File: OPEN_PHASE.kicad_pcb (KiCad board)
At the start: 4 copper layers, 65 x 77.5 mm, 117 parts, among them IC1 AD7606C-18BSTZ, IC10 INA241A2IDGKR, IC2 INA241A2IDGKR, IC3 LTC6655BHMS8-2.5#PBF, IC4 INA241A2IDGKR, IC5 LT8362EMSE#PBF, IC6 INA241A2IDGKR, IC7 LTC6655BHMS8-5#PBF, IC8 LT3045EDD-1#TRPBF, IC9 LT3045EDD-1#TRPBF, J1 MR60PW, J2 MR60PW, J3 XT60PW-F, J4 PinHeader_2x08, J5 XT60PW-M

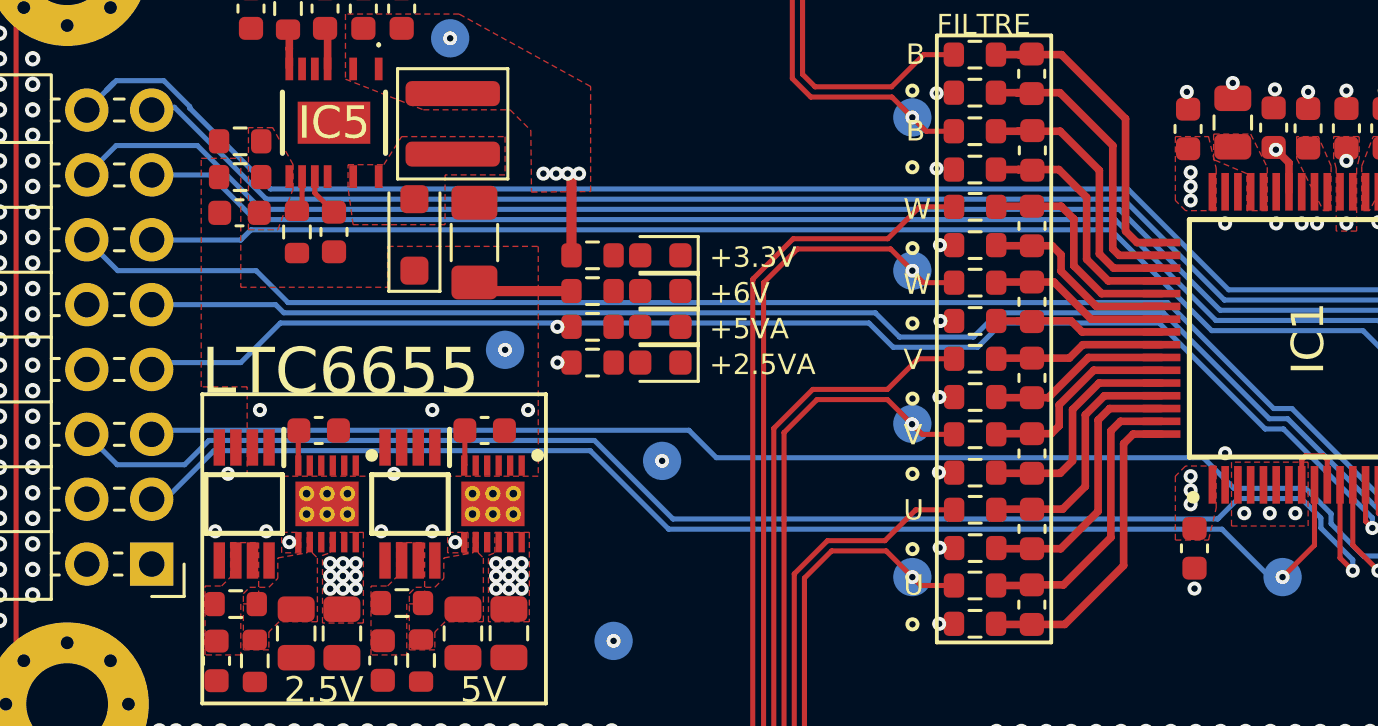
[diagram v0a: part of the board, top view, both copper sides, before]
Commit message: Add 100 Ohm series resistors on the J4 lines, bottom side
RN1, RN2 (R_Array_Concave_4x0603, the 4 x 100 Ohm array of OPEN_WEIGHT)
and R39-R41 (0603) sit inline on the existing B.Cu buses between IC1 and
J4; only the bus sections around them were redrawn. Element order follows
the routing: RN2 = DOUTD..DOUTA, R41 = SDI, RN1 = FRSTDATA, SCLK, CS,
BUSY, R40 = RESET, R39 = CONVST. J4 pinout unchanged.

Schematic: IC1 keeps its wires with local labels (IC side); the resistor
block carries the ADC_* global labels (J4 side). TP15 / TP16 move to the
IC side, where their pads are on the board.

Fixes a short: the +5VA via of R36 (138.6, 60.2) sat on the ADC_~{CS}
track; bus B now passes above it.

DRC 206 -> 203 (the short's 3 errors), parity 34 -> 16 (all pre-existing),
ERC unchanged; top and inner layers identical.

Co-Authored-By: Claude Opus 5.5 <noreply@anthropic.com>
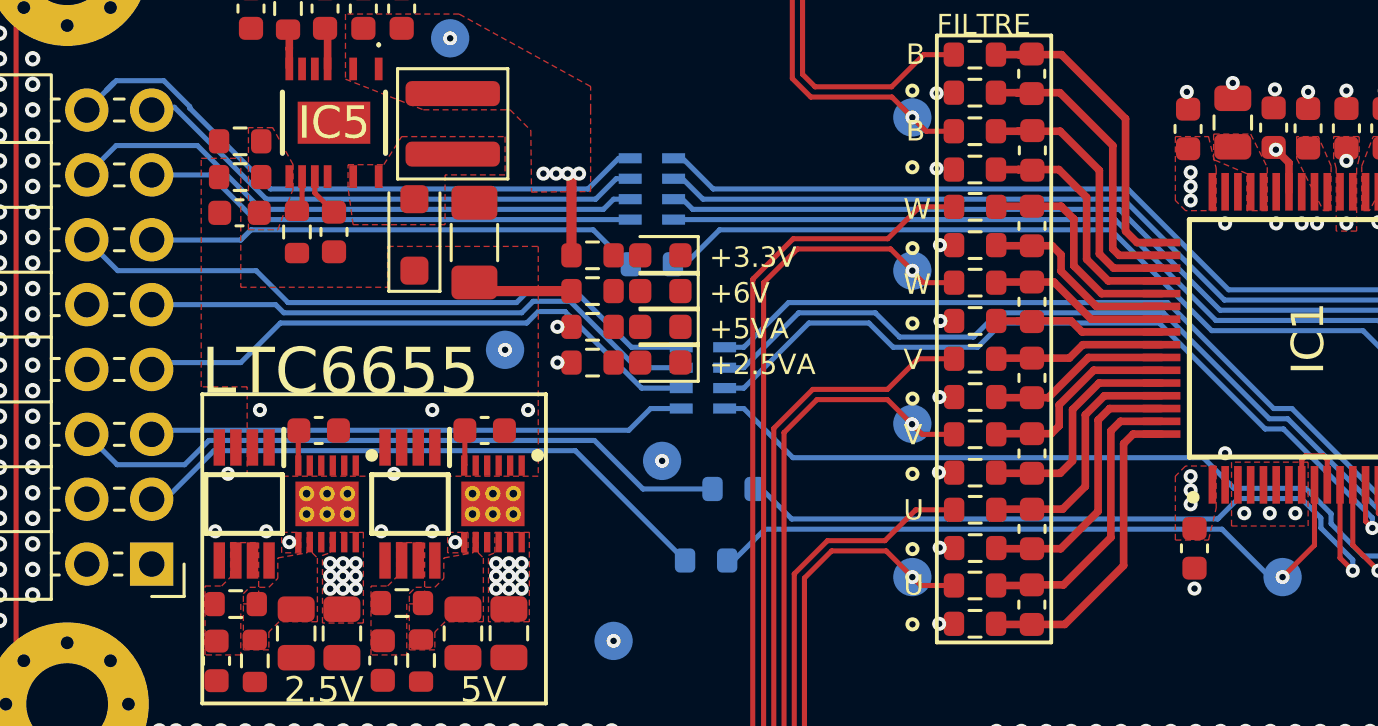
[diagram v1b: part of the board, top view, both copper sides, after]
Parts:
- added R39: 100Ω, OPEN_PHASE:R_0603_1608Metric, B.Cu at (144.4, 69.3)
- added R40: 100Ω, OPEN_PHASE:R_0603_1608Metric, B.Cu at (145.5, 66.5)
- added R41: 100Ω, OPEN_PHASE:R_0603_1608Metric, B.Cu at (142.3, 57.8)
- added RN1: RP_100Ω, OPEN_PHASE:R_Array_Concave_4x0603, B.Cu at (144.3, 62.2)
- added RN2: RP_100Ω, OPEN_PHASE:R_Array_Concave_4x0603, B.Cu at (142.3, 54.8)
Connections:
- IC1 pad 11: ADC_RESET -> /Project Architecture/AD7606C-18_ADC/RESET
- IC1 pad 12: ADC_SCLK -> /Project Architecture/AD7606C-18_ADC/SCLK
- IC1 pad 13: ADC_~{CS} -> /Project Architecture/AD7606C-18_ADC/~{CS}
- IC1 pad 14: ADC_BUSY -> /Project Architecture/AD7606C-18_ADC/BUSY
- IC1 pad 15: ADC_FRSTDATA -> /Project Architecture/AD7606C-18_ADC/FRSTDATA
- IC1 pad 24: ADC_DOUTA -> /Project Architecture/AD7606C-18_ADC/DOUTA
- IC1 pad 25: ADC_DOUTB -> /Project Architecture/AD7606C-18_ADC/DOUTB
- IC1 pad 27: ADC_DOUTC -> /Project Architecture/AD7606C-18_ADC/DOUTC
- IC1 pad 28: ADC_DOUTD -> /Project Architecture/AD7606C-18_ADC/DOUTD
- IC1 pad 29: ADC_SDI -> /Project Architecture/AD7606C-18_ADC/SDI
- IC1 pad 9: ADC_CONVST -> /Project Architecture/AD7606C-18_ADC/CONVST
- TP15 pad 1: ADC_CONVST -> /Project Architecture/AD7606C-18_ADC/CONVST
- TP16 pad 1: ADC_BUSY -> /Project Architecture/AD7606C-18_ADC/BUSY
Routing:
- net ADC_SDI: track 64.4 -> 19.5 mm, vias 1 -> 0
- net /Project Architecture/AD7606C-18_ADC/SDI: track 0.00 -> 44.4 mm, vias 0 -> 1
- net /Project Architecture/AD7606C-18_ADC/SCLK: track 0.00 -> 42.8 mm, vias 0 -> 1
- net ADC_SCLK: track 64.5 -> 22.1 mm, vias 1 -> 0
- net ADC_DOUTC: track 60.1 -> 20.6 mm, vias 1 -> 0
- net ADC_DOUTB: track 62.4 -> 23.0 mm, vias 1 -> 0
- net /Project Architecture/AD7606C-18_ADC/DOUTC: track 0.00 -> 38.5 mm, vias 0 -> 1
- net ADC_DOUTD: track 63.0 -> 24.9 mm, vias 1 -> 0
- net /Project Architecture/AD7606C-18_ADC/DOUTB: track 0.00 -> 38.1 mm, vias 0 -> 1
- net /Project Architecture/AD7606C-18_ADC/DOUTD: track 0.00 -> 37.4 mm, vias 0 -> 1
- net ADC_BUSY: track 56.7 -> 21.2 mm, vias 1 -> 0
- net /Project Architecture/AD7606C-18_ADC/BUSY: track 0.00 -> 34.5 mm, vias 0 -> 1
- net ADC_DOUTA: track 53.8 -> 19.5 mm, vias 1 -> 0
- net /Project Architecture/AD7606C-18_ADC/FRSTDATA: track 0.00 -> 33.3 mm, vias 0 -> 1
- net ADC_FRSTDATA: track 58.6 -> 25.4 mm, vias 1 -> 0
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
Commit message: Add 100k pull-up on ADC CS and pull-downs on CONVST and RESET
R42 (CS to +3.3V), R43 (CONVST to GND) and R44 (RESET to GND), 100k 0603
on the AD7606C side, as R8 on OPEN_WEIGHT: the lines stay in a known state
while the host does not drive them (MCU in reset, wire unplugged).

Bottom side: R43 and R44 go straight into the B.Cu GND pour; R44 sits at
the east end of the BUSY / RESET band so the band stays connected. R42
reaches +3.3V through a new via at (165.8, 64.7) into the In2 +3.3V
branch, under the IC1 corner (only that via's clearance changes on F.Cu
and In1).

DRC 203 = 203, unconnected 4 = 4, parity 16 = 16, ERC unchanged.

Co-Authored-By: Claude Opus 5.5 <noreply@anthropic.com>
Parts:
- added R42: 100kΩ, OPEN_PHASE:R_0603_1608Metric, B.Cu at (161.5, 63.0)
- added R43: 100kΩ, OPEN_PHASE:R_0603_1608Metric, B.Cu at (157.0, 69.6)
- added R44: 100kΩ, OPEN_PHASE:R_0603_1608Metric, B.Cu at (161.6, 66.5)
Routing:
- net +3.3V: track 7.64 -> 11.8 mm, vias 9 -> 10
- net /Project Architecture/AD7606C-18_ADC/~{CS}: track 32.6 -> 35.5 mm
- net /Project Architecture/AD7606C-18_ADC/RESET: track 29.5 -> 30.7 mm
- net /Project Architecture/AD7606C-18_ADC/CONVST: track 27.2 -> 27.8 mm
